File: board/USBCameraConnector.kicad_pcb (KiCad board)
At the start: 2 copper layers, 13.2 x 10.2 mm, 7 parts, among them J1 USB4105-GF-A, J7 Conn_01x04_Pin

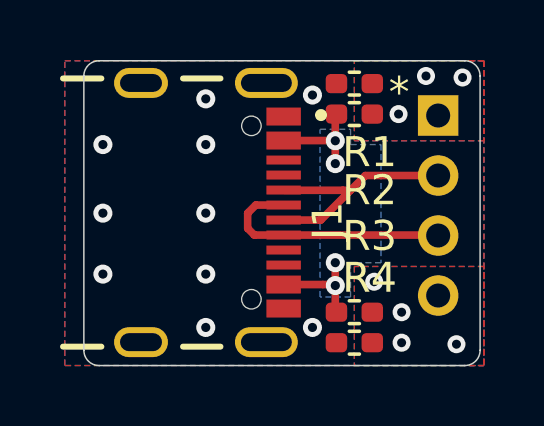
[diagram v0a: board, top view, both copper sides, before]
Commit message: Better GND vias
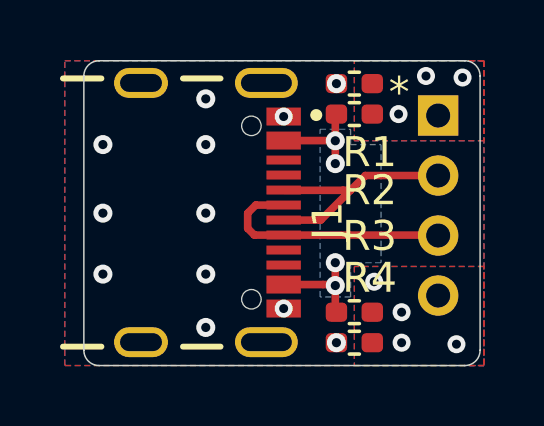
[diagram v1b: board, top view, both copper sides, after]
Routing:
- net GND: vias 10 -> 12
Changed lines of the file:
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@@
 		)
 		(fp_circle
-			(center -3.25 -6)
-			(end -3.15 -6)
+			(center -3.25 -5.842)
+			(end -3.15 -5.842)
 			(stroke
 				(width 0.2)
@@
 		)
 		(fp_circle
-			(center -3.25 -6)
-			(end -3.15 -6)
+			(center -3.25 -5.842)
+			(end -3.15 -5.842)
 			(stroke
 				(width 0.2)
@@
 	)
 	(via
+		(at 135.819 76.79)
+		(size 0.6)
+		(drill 0.3)
+		(layers "F.Cu" "B.Cu")
+		(net 7)
+	)
+	(via
 		(at 129.794 77.724)
 		(size 0.635)
@@
 	)
 	(via
-		(at 136.779 83.82)
+		(at 137.5785 84.328)
 		(size 0.635)
 		(drill 0.3048)
@@
 	)
 	(via
-		(at 136.779 76.073)
+		(at 137.5785 75.692)
 		(size 0.635)
 		(drill 0.3048)
@@
 		(net 7)
 	)
+	(via
+		(at 135.819 83.19)
+		(size 0.6)
+		(drill 0.3)
+		(layers "F.Cu" "B.Cu")
+		(net 7)
+	)
